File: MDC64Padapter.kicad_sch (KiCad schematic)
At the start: 33 parts, among them J1 DB9_F_TO_C64, J2 DB9_M_TO_PAD, Q1 BC547, Q2 BC547, SW1 MODE, U1 74AHCT1G08, U2 74ACT373, U3 74AC157, U4 74ACT373, U5 74AHC1G04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

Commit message: Update
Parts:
- removed U1: 74AHCT1G08, symbol 74xGxx:74AHC1G08
- added U1: 74ACT08, symbol 74xx:74LS08
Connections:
- net C64_UP: now also U1.2
- net GND: now also U1.10, U1.12, U1.13, U1.7 (GND), U1.9
- net MD_A: now also U1.4; no longer U3.11 (I0c)
- net MD_C: now also U1.1
- net MD_START: now also U1.5
- net VCC: now also U1.14 (VCC)
- net at U3.3 (I1a): now also U1.3
- new net: U1.6, U3.11 (I0c)
- no-connect marks 13 -> 15

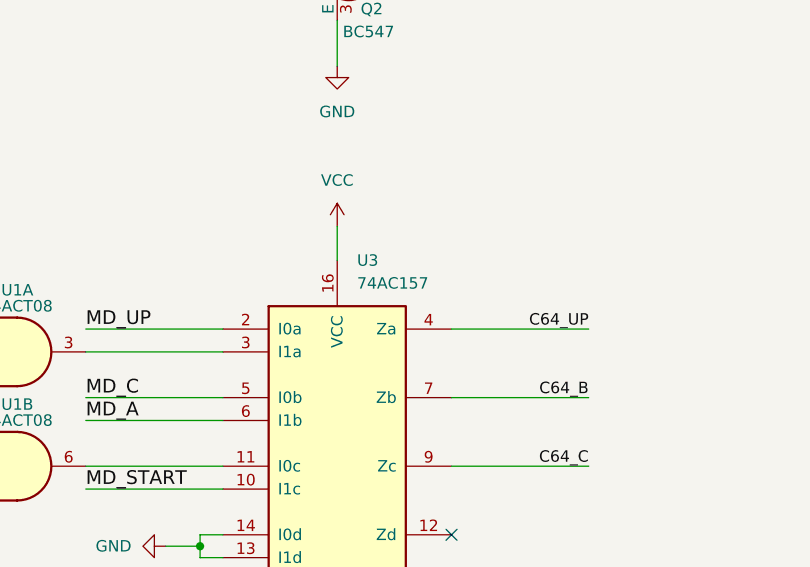
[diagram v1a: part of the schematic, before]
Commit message: Use a cmos mux
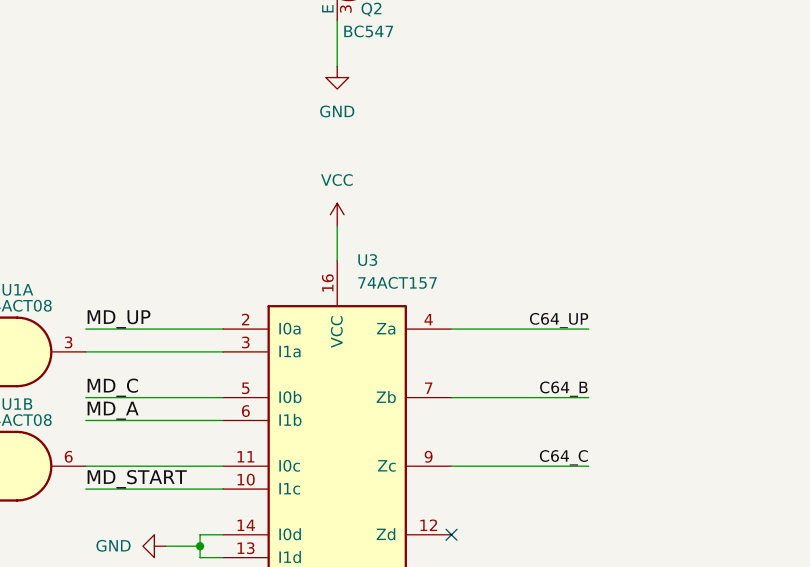
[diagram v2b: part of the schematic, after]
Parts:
- U3: value 74AC157 -> 74ACT157
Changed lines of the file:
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@@
 			)
 		)
-		(property "Value" "74AC157"
+		(property "Value" "74ACT157"
 			(at 102.5241 72.39 0)
 			(effects

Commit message: Begin placing components on the PCB
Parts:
- removed Q1, Q2: BC547, Package_TO_SOT_THT:TO-92_HandSolder, symbol OpenC64MegaDrivePadAdapter-rescue:BC547
- added Q1, Q2: BC847, Package_TO_SOT_SMD:SOT-23, symbol Transistor_BJT:BC847
- added R9: 10K, Resistor_SMD:R_1206_3216Metric_Pad1.30x1.75mm_HandSolder, symbol Device:R_Small
- C3, C4, C5, C6, C7: footprint (none) -> Capacitor_SMD:C_1206_3216Metric_Pad1.33x1.80mm_HandSolder
- D1, D2, D3, D4, D5: footprint Diode_THT:D_DO-35_SOD27_P7.62mm_Horizontal -> Diode_SMD:D_SOD-123F
- R1, R2, R3, R4, R5, R6: footprint Resistor_THT:R_Axial_DIN0204_L3.6mm_D1.6mm_P7.62mm_Horizontal -> Resistor_SMD:R_1206_3216Metric_Pad1.30x1.75mm_HandSolder
- RN1, RN2: footprint (none) -> Resistor_SMD:R_Array_Convex_4x0612
- SW1: footprint Button_Switch_SMD:SW_SPDT_CK-JS102011SAQN -> Button_Switch_SMD:SW_SPDT_CK_JS102011SAQN
- U1: footprint (none) -> Package_SO:TSSOP-14_4.4x5mm_P0.65mm
- U2: footprint (none) -> Package_SO:SSOP-20_5.3x7.2mm_P0.65mm; Mouser (none) -> https://www.mouser.it/ProductDetail/Texas-Instruments/SN74A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
- U3: footprint (none) -> Package_SO:TSSOP-16_4.4x5mm_P0.65mm
- U4: footprint (none) -> Package_SO:SSOP-20_5.3x7.2mm_P0.65mm
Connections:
- net C64_POTX: now also Q2.3 (C)
- net C64_POTY: now also Q1.3 (C)
- net C64_UP: now also U1.1; no longer U1.2
- net GND: now also C3.2, C4.2, C6.2, C7.2, Q1.2 (E), Q2.2 (E), R9.2
- net MD_B/~{A}: now also RN1.7 (R2.2), RN2.7 (R2.2); no longer RN1.6 (R3.2), RN2.6 (R3.2)
- net MD_C: now also U1.2; no longer U1.1
- net MD_C/~{ST}: now also RN1.8 (R1.2), RN2.8 (R1.2); no longer RN1.5 (R4.2), RN2.5 (R4.2)
- net MD_LEFT_M: now also RN1.6 (R3.2); no longer RN1.7 (R2.2)
- net MD_RIGHT_M: now also RN1.5 (R4.2); no longer RN1.8 (R1.2)
- net VCC: now also C3.1, C4.1, C6.1, C7.1
- net at SW1.2 (B), U3.1 (S): now also R9.1; no longer RN2.8 (R1.2)
- net at R5.1, R6.2: now also Q2.1 (B)
- net at R2.1, R3.2: now also Q1.1 (B)
- no-connect marks 15 -> 16

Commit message: Reorganize pcb a bit
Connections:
- net C64_DOWN: now also RN1.7 (R2.2)
- net C64_UP: now also RN1.5 (R4.2)
- net GND: no longer RN1.1 (R1.1), RN1.2 (R2.1), RN1.3 (R3.1), RN1.4 (R4.1), RN2.1 (R1.1), RN2.2 (R2.1), RN2.3 (R3.1), RN2.4 (R4.1)
- net MD_B/~{A}: now also RN1.6 (R3.2); no longer RN1.7 (R2.2), RN2.7 (R2.2)
- net MD_C/~{ST}: no longer RN1.8 (R1.2)
- net MD_LEFT_M: now also RN1.8 (R1.2); no longer RN1.6 (R3.2)
- net MD_RIGHT_M: now also RN2.7 (R2.2); no longer RN1.5 (R4.2)
- net VCC: now also RN1.1 (R1.1), RN1.2 (R2.1), RN1.3 (R3.1), RN1.4 (R4.1), RN2.1 (R1.1), RN2.2 (R2.1), RN2.3 (R3.1), RN2.4 (R4.1)
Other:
- moved on the sheet: C3, C4, C5, C6, C7, RN1, RN2

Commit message: First PCB design
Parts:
- U5: footprint (none) -> Package_TO_SOT_SMD:SOT-353_SC-70-5_Handsoldering
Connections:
- net C64_B: now also U3.9 (Zc); no longer U3.7 (Zb)
- net C64_C: now also U3.7 (Zb); no longer U3.9 (Zc)
- net MD_A: now also U3.10 (I1c); no longer U3.6 (I1b)
- net MD_C: now also U3.11 (I0c); no longer U3.5 (I0b)
- net MD_C/~{ST}: now also RN2.6 (R3.2); no longer RN2.8 (R1.2)
- net MD_RIGHT_M: now also RN2.5 (R4.2); no longer RN2.7 (R2.2)
- net MD_START: now also U3.6 (I1b); no longer U3.10 (I1c)
- net at U1.6: now also U3.5 (I0b); no longer U3.11 (I0c)
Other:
- moved on the sheet: U1A, U1B
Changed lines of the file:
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@@
 	)
 	(no_connect
+		(at 241.3 49.53)
+	)
+	(no_connect
 		(at 76.2 158.75)
 	)
@@
 	)
 	(no_connect
-		(at 248.92 49.53)
+		(at 243.84 49.53)
 	)
 	(no_connect
@@
 		(at 76.2 163.83)
 	)
-	(no_connect
-		(at 246.38 49.53)
-	)
 	(wire
 		(pts
@@
 	(wire
 		(pts
-			(xy 266.7 109.22) (xy 266.7 132.08)
+			(xy 72.39 87.63) (xy 87.63 87.63)
 		)
 		(stroke
@@
 	(wire
 		(pts
-			(xy 72.39 95.25) (xy 87.63 95.25)
+			(xy 266.7 109.22) (xy 266.7 132.08)
 		)
 		(stroke
@@
 	(wire
 		(pts
-			(xy 72.39 85.09) (xy 87.63 85.09)
+			(xy 72.39 92.71) (xy 87.63 92.71)
 		)
 		(stroke
@@
 	(wire
 		(pts
-			(xy 100.33 30.48) (xy 100.33 33.02)
+			(xy 45.72 87.63) (xy 66.04 87.63)
 		)
 		(stroke
@@
 	(wire
 		(pts
-			(xy 241.3 45.72) (xy 241.3 26.67)
+			(xy 100.33 30.48) (xy 100.33 33.02)
 		)
 		(stroke
@@
 	(wire
 		(pts
-			(xy 266.7 142.24) (xy 259.08 142.24)
+			(xy 241.3 45.72) (xy 241.3 26.67)
 		)
 		(stroke
@@
 	(wire
 		(pts
-			(xy 260.35 36.83) (xy 266.7 36.83)
+			(xy 266.7 142.24) (xy 259.08 142.24)
 		)
 		(stroke
@@
 	(wire
 		(pts
-			(xy 163.83 35.56) (xy 177.8 35.56)
+			(xy 260.35 36.83) (xy 266.7 36.83)
 		)
 		(stroke
@@
 	(wire
 		(pts
-			(xy 262.89 60.96) (xy 265.43 60.96)
+			(xy 163.83 35.56) (xy 177.8 35.56)
 		)
 		(stroke
@@
 	(wire
 		(pts
-			(xy 48.26 38.1) (xy 53.34 38.1)
+			(xy 262.89 60.96) (xy 265.43 60.96)
 		)
 		(stroke
@@
 	(wire
 		(pts
-			(xy 243.84 49.53) (xy 243.84 45.72)
+			(xy 48.26 38.1) (xy 53.34 38.1)
 		)
 		(stroke
@@
 	(wire
 		(pts
-			(xy 72.39 80.01) (xy 87.63 80.01)
-		)
-		(stroke
-			(width 0)
-			(type default)
-		)
-	)
-	(wire
-		(pts
-			(xy 72.39 87.63) (xy 87.63 87.63)
+			(xy 72.39 95.25) (xy 87.63 95.25)
 		)
 		(stroke
@@
 	(wire
 		(pts
+			(xy 44.45 74.93) (xy 66.04 74.93)
+		)
+		(stroke
+			(width 0)
+			(type default)
+		)
+	)
+	(wire
+		(pts
+			(xy 66.04 74.93) (xy 66.04 80.01)
+		)
+		(stroke
+			(width 0)
+			(type default)
+		)
+	)
+	(wire
+		(pts
 			(xy 229.87 137.16) (xy 233.68 137.16)
 		)
@@
 	(wire
 		(pts
+			(xy 248.92 45.72) (xy 248.92 49.53)
+		)
+		(stroke
+			(width 0)
+			(type default)
+		)
+	)
+	(wire
+		(pts
 			(xy 133.35 156.21) (xy 135.89 156.21)
 		)
@@
 	(wire
 		(pts
-			(xy 48.26 77.47) (xy 57.15 77.47)
+			(xy 20.32 72.39) (xy 29.21 72.39)
 		)
 		(stroke
@@
 	(wire
 		(pts
+			(xy 246.38 46.99) (xy 246.38 49.53)
+		)
+		(stroke
+			(width 0)
+			(type default)
+		)
+	)
+	(wire
+		(pts
 			(xy 246.38 59.69) (xy 246.38 60.96)
 		)
@@
 	(wire
 		(pts
-			(xy 241.3 46.99) (xy 240.03 46.99)
+			(xy 240.03 46.99) (xy 246.38 46.99)
+		)
+		(stroke
+			(width 0)
+			(type default)
+		)
+	)
+	(wire
+		(pts
+			(xy 66.04 87.63) (xy 66.04 85.09)
 		)
 		(stroke
@@
 	(wire
 		(pts
-			(xy 243.84 45.72) (xy 241.3 45.72)
+			(xy 66.04 85.09) (xy 87.63 85.09)
+		)
+		(stroke
+			(width 0)
+			(type default)
+		)
+	)
+	(wire
+		(pts
+			(xy 241.3 45.72) (xy 248.92 45.72)
 		)
 		(stroke
@@
 	(wire
 		(pts
-			(xy 45.72 95.25) (xy 57.15 95.25)
+			(xy 19.05 90.17) (xy 30.48 90.17)
 		)
 		(stroke
@@
 	(wire
 		(pts
-			(xy 72.39 92.71) (xy 87.63 92.71)
+			(xy 257.81 49.53) (xy 257.81 44.45)
 		)
 		(stroke
@@
 	(wire
 		(pts
-			(xy 257.81 49.53) (xy 257.81 44.45)
+			(xy 63.5 184.15) (xy 63.5 185.42)
 		)
 		(stroke
@@
 	(wire
 		(pts
-			(xy 63.5 184.15) (xy 63.5 185.42)
+			(xy 163.83 40.64) (xy 177.8 40.64)
 		)
 		(stroke
@@
 	(wire
 		(pts
-			(xy 163.83 40.64) (xy 177.8 40.64)
+			(xy 66.04 80.01) (xy 87.63 80.01)
 		)
 		(stroke
@@
 	(wire
 		(pts
-			(xy 113.03 92.71) (xy 128.27 92.71)
+			(xy 113.03 85.09) (xy 128.27 85.09)
 		)
 		(stroke
@@
 	(wire
 		(pts
-			(xy 48.26 82.55) (xy 57.15 82.55)
+			(xy 20.32 77.47) (xy 29.21 77.47)
 		)
 		(stroke
@@
 	(wire
 		(pts
-			(xy 45.72 90.17) (xy 57.15 90.17)
+			(xy 19.05 85.09) (xy 30.48 85.09)
 		)
 		(stroke
@@
 	(wire
 		(pts
-			(xy 241.3 49.53) (xy 241.3 46.99)
-		)
-		(stroke
-			(width 0)
-			(type default)
-		)
-	)
-	(wire
-		(pts
 			(xy 142.24 105.41) (xy 142.24 107.95)
 		)
@@
 	(wire
 		(pts
-			(xy 113.03 85.09) (xy 128.27 85.09)
+			(xy 113.03 92.71) (xy 128.27 92.71)
 		)
 		(stroke
@@
 	)
 	(label "C64_B"
-		(at 128.27 85.09 180)
+		(at 128.27 92.71 180)
 		(fields_autoplaced yes)
 		(effects
@@
 	)
 	(label "MD_START"
-		(at 72.39 95.25 0)
+		(at 72.39 87.63 0)
 		(fields_autoplaced yes)
 		(effects
@@
 	)
 	(label "MD_START"
-		(at 45.72 95.25 0)
+		(at 19.05 90.17 0)
 		(fields_autoplaced yes)
 		(effects
@@
 	)
 	(label "MD_A"
-		(at 45.72 90.17 0)
+		(at 19.05 85.09 0)
 		(fields_autoplaced yes)
 		(effects
@@
 	)
 	(label "MD_C"
-		(at 72.39 85.09 0)
+		(at 72.39 92.71 0)
 		(fields_autoplaced yes)
 		(effects
@@
 	)
 	(label "C64_C"
-		(at 128.27 92.71 180)
+		(at 128.27 85.09 180)
 		(fields_autoplaced yes)
 		(effects
@@
 	)
 	(label "MD_UP"
-		(at 48.26 77.47 0)
+		(at 20.32 72.39 0)
 		(fields_autoplaced yes)
 		(effects
@@
 	)
 	(label "MD_C"
-		(at 48.26 82.55 0)
+		(at 20.32 77.47 0)
 		(fields_autoplaced yes)
 		(effects
@@
 	)
 	(label "MD_A"
-		(at 72.39 87.63 0)
+		(at 72.39 95.25 0)
 		(fields_autoplaced yes)
 		(effects
@@
 			)
 		)
-		(property "Footprint" ""
+		(property "Footprint" "Package_TO_SOT_SMD:SOT-353_SC-70-5_Handsoldering"
 			(at 227.33 109.22 0)
 			(effects
@@
 	(symbol
 		(lib_id "74xx:74LS08")
-		(at 64.77 92.71 0)
+		(at 38.1 87.63 0)
 		(unit 2)
 		(exclude_from_sim no)
@@
 		(dnp no)
 		(property "Reference" "U1"
-			(at 64.7783 85.852 0)
+			(at 38.1083 80.772 0)
 			(effects
 				(font
@@
 		)
 		(property "Value" "74ACT08"
-			(at 64.77 87.63 0)
+			(at 38.1 82.55 0)
 			(effects
 				(font
@@
 		)
 		(property "Footprint" "Package_SO:TSSOP-14_4.4x5mm_P0.65mm"
-			(at 64.77 92.71 0)
+			(at 38.1 87.63 0)
 			(effects
 				(font
@@
 		)
 		(property "Datasheet" "http://www.ti.com/lit/gpn/sn74LS08"
-			(at 64.77 92.71 0)
+			(at 38.1 87.63 0)
 			(effects
 				(font
@@
 		)
 		(property "Description" "Quad And2"
-			(at 64.77 92.71 0)
+			(at 38.1 87.63 0)
 			(effects
 				(font
@@
 	(symbol
 		(lib_id "74xx:74LS08")
-		(at 64.77 80.01 0)
+		(at 36.83 74.93 0)
 		(unit 1)
 		(exclude_from_sim no)
@@
 		(dnp no)
 		(property "Reference" "U1"
-			(at 64.7783 73.152 0)
+			(at 36.8383 68.072 0)
 			(effects
 				(font
@@
 		)
 		(property "Value" "74ACT08"
-			(at 64.77 74.93 0)
+			(at 36.83 69.85 0)
 			(effects
 				(font
@@
 		)
 		(property "Footprint" "Package_SO:TSSOP-14_4.4x5mm_P0.65mm"
-			(at 64.77 80.01 0)
+			(at 36.83 74.93 0)
 			(effects
 				(font
@@
 		)
 		(property "Datasheet" "http://www.ti.com/lit/gpn/sn74LS08"
-			(at 64.77 80.01 0)
+			(at 36.83 74.93 0)
 			(effects
 				(font
@@
 		)
 		(property "Description" "Quad And2"
-			(at 64.77 80.01 0)
+			(at 36.83 74.93 0)
 			(effects
 				(font

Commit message: Add amiga compatibility
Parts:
- added JP1: Amiga/C64 SEL1, Jumper:SolderJumper-3_P1.3mm_Open_RoundedPad1.0x1.5mm, symbol Jumper:Jumper_3_Open
- added JP2: Amiga/C64 SEL2, Jumper:SolderJumper-3_P1.3mm_Open_RoundedPad1.0x1.5mm, symbol Jumper:Jumper_3_Open
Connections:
- net C64_B: now also JP2.1 (A)
- net C64_C: now also JP1.1 (A)
- net C64_POTX: now also JP2.2 (C); no longer Q2.3 (C), R4.2, R5.2
- net C64_POTY: now also JP1.2 (C); no longer Q1.3 (C), R1.2, R2.2
- new net: JP1.3 (B), Q1.3 (C), R1.2, R2.2
- new net: JP2.3 (B), Q2.3 (C), R4.2, R5.2
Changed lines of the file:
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@@
 	(wire
 		(pts
+			(xy 27.94 30.48) (xy 31.75 30.48)
+		)
+		(stroke
+			(width 0)
+			(type default)
+		)
+	)
+	(wire
+		(pts
 			(xy 48.26 158.75) (xy 48.26 161.29)
 		)
@@
 	(wire
 		(pts
+			(xy 81.28 30.48) (xy 81.28 48.26)
+		)
+		(stroke
+			(width 0)
+			(type default)
+		)
+	)
+	(wire
+		(pts
 			(xy 252.73 60.96) (xy 257.81 60.96)
 		)
@@
 	(wire
 		(pts
+			(xy 87.63 52.07) (xy 87.63 63.5)
+		)
+		(stroke
+			(width 0)
+			(type default)
+		)
+	)
+	(wire
+		(pts
 			(xy 265.43 41.91) (xy 266.7 41.91)
 		)
@@
 	(wire
 		(pts
+			(xy 27.94 48.26) (xy 27.94 30.48)
+		)
+		(stroke
+			(width 0)
+			(type default)
+		)
+	)
+	(wire
+		(pts
 			(xy 66.04 87.63) (xy 66.04 85.09)
 		)
@@
 	(wire
 		(pts
+			(xy 95.25 48.26) (xy 93.98 48.26)
+		)
+		(stroke
+			(width 0)
+			(type default)
+		)
+	)
+	(wire
+		(pts
 			(xy 153.67 113.03) (xy 153.67 115.57)
 		)
@@
 	(wire
 		(pts
+			(xy 95.25 30.48) (xy 95.25 48.26)
+		)
+		(stroke
+			(width 0)
+			(type default)
+		)
+	)
+	(wire
+		(pts
 			(xy 241.3 45.72) (xy 248.92 45.72)
 		)
@@
 	(wire
 		(pts
-			(xy 13.97 38.1) (xy 26.67 38.1)
+			(xy 161.29 148.59) (xy 180.34 148.59)
 		)
 		(stroke
@@
 	(wire
 		(pts
-			(xy 161.29 148.59) (xy 180.34 148.59)
+			(xy 15.24 30.48) (xy 15.24 48.26)
 		)
 		(stroke
@@
 	(wire
 		(pts
-			(xy 95.25 30.48) (xy 95.25 38.1)
-		)
-		(stroke
-			(width 0)
-			(type default)
-		)
-	)
-	(wire
-		(pts
 			(xy 161.29 151.13) (xy 180.34 151.13)
 		)
@@
 	(wire
 		(pts
+			(xy 21.59 52.07) (xy 21.59 63.5)
+		)
+		(stroke
+			(width 0)
+			(type default)
+		)
+	)
+	(wire
+		(pts
 			(xy 100.33 120.65) (xy 81.28 120.65)
 		)
@@
 	(wire
 		(pts
-			(xy 82.55 38.1) (xy 95.25 38.1)
-		)
-		(stroke
-			(width 0)
-			(type default)
-		)
-	)
-	(wire
-		(pts
 			(xy 260.35 59.69) (xy 260.35 60.96)
 		)
@@
 	(wire
 		(pts
-			(xy 26.67 30.48) (xy 26.67 38.1)
-		)
-		(stroke
-			(width 0)
-			(type default)
-		)
-	)
-	(wire
-		(pts
 			(xy 257.81 60.96) (xy 260.35 60.96)
 		)
@@
 	(wire
 		(pts
-			(xy 31.75 30.48) (xy 26.67 30.48)
-		)
-		(stroke
-			(width 0)
-			(type default)
-		)
-	)
-	(wire
-		(pts
 			(xy 76.2 156.21) (xy 95.25 156.21)
 		)
@@
 		)
 	)
+	(label "C64_POTY"
+		(at 21.59 63.5 90)
+		(fields_autoplaced yes)
+		(effects
+			(font
+				(size 1.524 1.524)
+			)
+			(justify left bottom)
+		)
+	)
 	(label "MD_DOWN"
 		(at 233.68 35.56 180)
@@
 	)
 	(label "C64_B"
+		(at 81.28 30.48 270)
+		(fields_autoplaced yes)
+		(effects
+			(font
+				(size 1.27 1.27)
+			)
+			(justify right bottom)
+		)
+	)
+	(label "C64_B"
 		(at 128.27 92.71 180)
 		(fields_autoplaced yes)
@@
 		)
 	)
-	(label "MD_RIGHT"
-		(at 95.25 156.21 180)
+	(label "C64_C"
+		(at 15.24 30.48 270)
 		(fields_autoplaced yes)
 		(effects
@@
 		)
 	)
-	(label "C64_POTY"
-		(at 13.97 38.1 0)
-		(fields_autoplaced yes)
-		(effects
-			(font
-				(size 1.524 1.524)
-			)
-			(justify left bottom)
-		)
-	)
-	(label "C64_POTX"
-		(at 82.55 38.1 0)
+	(label "MD_RIGHT"
+		(at 95.25 156.21 180)
 		(fields_autoplaced yes)
 		(effects
 			(font
-				(size 1.524 1.524)
+				(size 1.27 1.27)
 			)
-			(justify left bottom)
+			(justify right bottom)
 		)
 	)
@@
 		)
 	)
+	(label "C64_POTX"
+		(at 87.63 63.5 90)
+		(fields_autoplaced yes)
+		(effects
+			(font
+				(size 1.524 1.524)
+			)
+			(justify left bottom)
+		)
+	)
 	(label "MD_B{slash}~{A}"
 		(at 115.57 151.13 0)
@@
 	)
 	(symbol
+		(lib_id "Jumper:Jumper_3_Open")
+		(at 87.63 48.26 0)
+		(unit 1)
+		(exclude_from_sim yes)
+		(in_bom no)
+		(on_board yes)
+		(dnp no)
+		(property "Reference" "JP2"
+			(at 81.534 57.404 90)
+			(effects
+				(font
+					(size 1.27 1.27)
+				)
+			)
+		)
+		(property "Value" "Amiga/C64 SEL2"
+			(at 84.074 57.404 90)
+			(effects
+				(font
+					(size 1.27 1.27)
+				)
+			)
+		)
+		(property "Footprint" "Jumper:SolderJumper-3_P1.3mm_Open_RoundedPad1.0x1.5mm"
+			(at 87.63 48.26 0)
+			(effects
+				(font
+					(size 1.27 1.27)
+				)
+				(hide yes)
+			)
+		)
+		(property "Datasheet" "~"
+			(at 87.63 48.26 0)
+			(effects
+				(font
+					(size 1.27 1.27)
+				)
+				(hide yes)
+			)
+		)
+		(property "Description" "Jumper, 3-pole, both open"
+			(at 87.63 48.26 0)
+			(effects
+				(font
+					(size 1.27 1.27)
+				)
+				(hide yes)
+			)
+		)
+		(pin "2"
+		)
+		(pin "1"
+		)
+		(pin "3"
+		)
+		(instances
+			(project "MDC64Padapter"
+				(path "/294adc81-b85b-4a2d-9150-4799a0ab7623"
+					(reference "JP2")
+					(unit 1)
+				)
+			)
+		)
+	)
+	(symbol
 		(lib_id "power:VCC")
 		(at 63.5 137.16 0)
@@
 					(unit 1)
 				)
+			)
+		)
+	)
+	(symbol
+		(lib_id "Jumper:Jumper_3_Open")
+		(at 21.59 48.26 0)
+		(unit 1)
+		(exclude_from_sim yes)
+		(in_bom no)
+		(on_board yes)
+		(dnp no)
+		(property "Reference" "JP1"
+			(at 15.494 57.404 90)
+			(effects
+				(font
+					(size 1.27 1.27)
+				)
+			)
+		)
+		(property "Value" "Amiga/C64 SEL1"
+			(at 18.034 57.404 90)
+			(effects
+				(font
+					(size 1.27 1.27)
+				)
+			)
+		)
+		(property "Footprint" "Jumper:SolderJumper-3_P1.3mm_Open_RoundedPad1.0x1.5mm"
+			(at 21.59 48.26 0)
+			(effects
+				(font
+					(size 1.27 1.27)
+				)
+				(hide yes)
+			)
+		)
+		(property "Datasheet" "~"
+			(at 21.59 48.26 0)
+			(effects
+				(font
+					(size 1.27 1.27)
+				)
+				(hide yes)
+			)
+		)
+		(property "Description" "Jumper, 3-pole, both open"
+			(at 21.59 48.26 0)
+			(effects
+				(font
+					(size 1.27 1.27)
+				)
+				(hide yes)
+			)
+		)
+		(pin "2"
+		)
+		(pin "1"
+		)
+		(pin "3"
+		)
+		(instances
+			(project ""
+				(path "/294adc81-b85b-4a2d-9150-4799a0ab7623"
+					(reference "JP1")
+					(unit 1)
+				)
